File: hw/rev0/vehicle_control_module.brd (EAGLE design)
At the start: 160 x 100 mm, 190 parts, among them IC1 SJA1105TELY, IC10 TJA1100HNZ, IC11 KSZ8061MNXI-TR, IC12 TJA1100HNZ, IC2 ATSAMV71Q21B-AABT, IC3 TJA1100HNZ, IC4 FT2232HL, IC5 TRS3232EQPWRQ1, IC6 AT24MAC402-XHM-B, IC7 DS3231SN#, IC8 TLE9252VSKXUMA1, J1 2305018-2, J10 5-2337992-3, J12 1017505, J2 2305018-2, J3 1017505, J4 1017505, J5 1017505, J6 1017505, J7 1017505, J8 1017505, J9 1017505, U1 122-2920-GR, Y1 NX3225SA-25MHZ-EXS00A-CS11338, Y2 NX2016SA-25.000M-STD-CZS-1

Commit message: Swap EEPROM with QSPI Flash, still has 48-bit EUI
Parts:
- added C64: 1uF, rcl:C0603
- added R78: 0, rcl:R0603
- added R79, R80, R81: 4.7k, rcl:R0603
- IC6: value AT24MAC402-XHM-B -> SST26VF032BT-104I_SM; device samacsys:SOP65P640X120-8N -> samacsys:SOIC127P794X203-8N
- moved IC6 804.9 mm to (-138.4, -853.4)
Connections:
- removed net VCC: IC7.2
- new net EXTINT_RTC: IC2.102, IC7.3, R81.1
- new net FLASH_WP: IC2.41, IC6.3, R78.1
- new net QSPI_QCS: IC2.64, IC6.1
- new net QSPI_QIO0: IC2.42, IC6.5
- new net QSPI_QIO1: IC2.68, IC6.2
- new net QSPI_QSCK: IC2.51, IC6.6
- net +3V3: now also C64.1, IC6.7, IC6.8, IC7.2, R78.2, R79.2, R80.2, R81.2
- net GND: now also C64.2, IC6.4, IC7.10, IC7.11, IC7.12, IC7.5, IC7.6, IC7.7, IC7.8, IC7.9, U1.3
- net I2C0_TWCK: now also IC7.16, R79.1
- net I2C0_TWD: now also IC7.15, R80.1

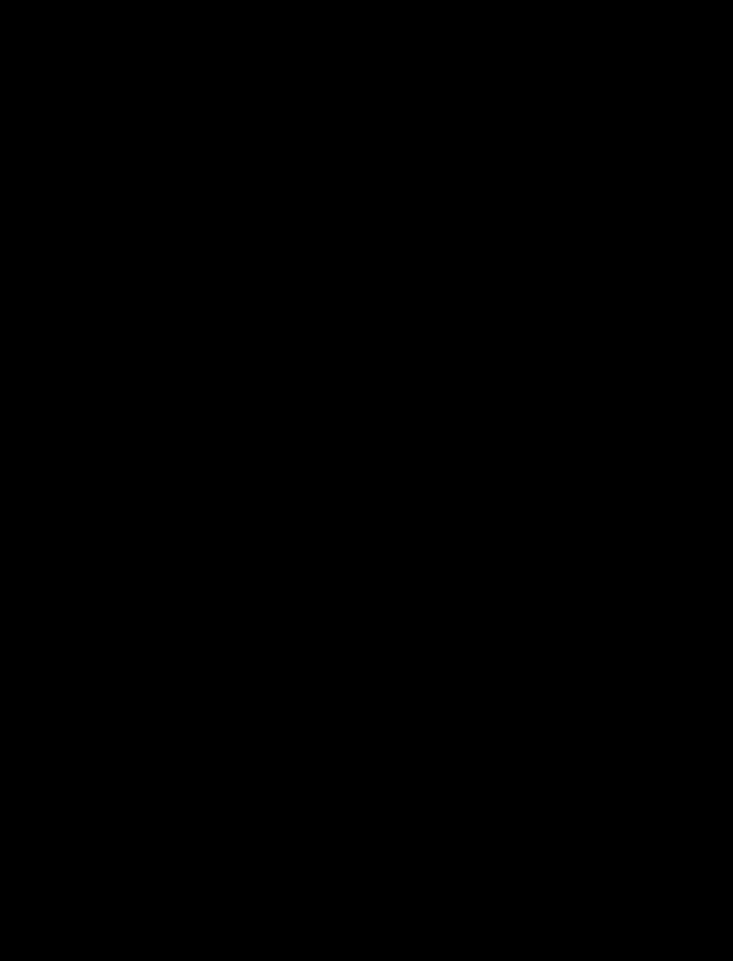
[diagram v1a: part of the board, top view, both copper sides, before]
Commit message: Add JTAG connector
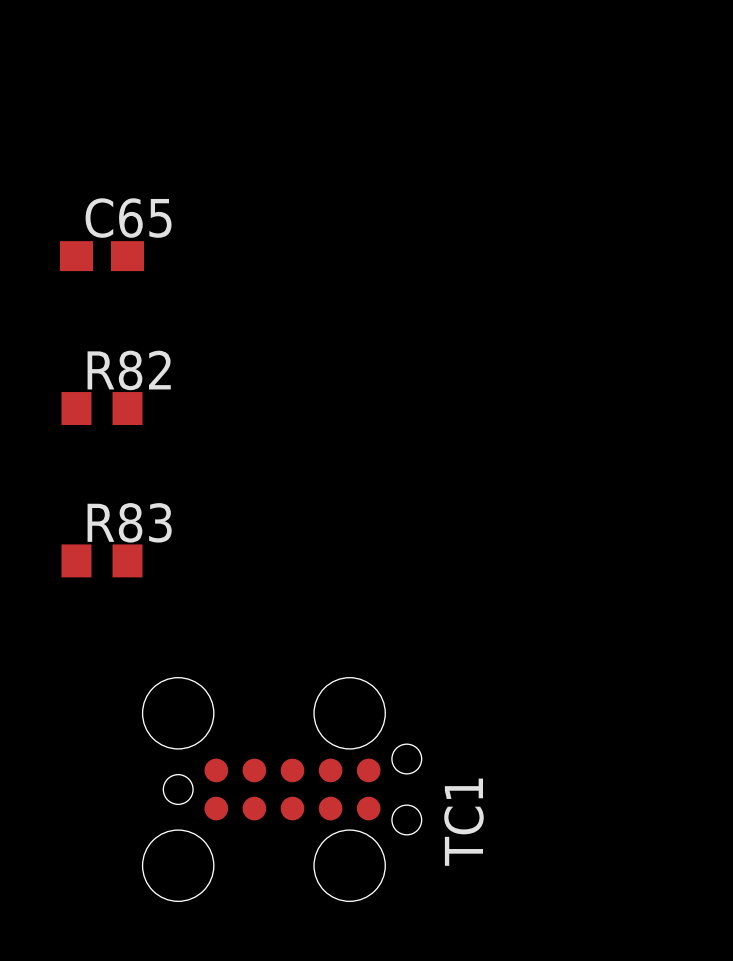
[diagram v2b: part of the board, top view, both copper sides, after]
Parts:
- added C65: 1uF, rcl:C0603
- added R82: 0, rcl:R0603
- added R83: 10k, rcl:R0603
- added TC1: TC2050-IDC, TagConnect:TC2050-IDC
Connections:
- new net HOST_RESET: IC2.83, R82.2, R83.2
- new net JTAG_NRST: R82.1, TC1.10
- new net JTAG_TCK: IC2.89, TC1.4, TC1.7
- new net JTAG_TDI: IC2.105, TC1.8
- new net JTAG_TDO: IC2.109, TC1.6
- new net JTAG_TMS: IC2.79, TC1.2
- new net V+: TC1.5
- net +3V3: now also R83.1, TC1.1
- net GND: now also TC1.3
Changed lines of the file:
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@@
 <layer number="48" name="Document" color="7" fill="1" visible="yes" active="yes"/>
 <layer number="49" name="Reference" color="7" fill="1" visible="yes" active="yes"/>
+<layer number="50" name="dxf" color="7" fill="1" visible="no" active="no"/>
 <layer number="51" name="tDocu" color="7" fill="1" visible="yes" active="yes"/>
 <layer number="52" name="bDocu" color="7" fill="1" visible="yes" active="yes"/>
@@
 <layer number="97" name="Info" color="7" fill="1" visible="no" active="no"/>
 <layer number="98" name="Guide" color="6" fill="1" visible="no" active="no"/>
+<layer number="200" name="200bmp" color="1" fill="10" visible="no" active="no"/>
+<layer number="250" name="Descript" color="3" fill="1" visible="no" active="no"/>
+<layer number="251" name="SMDround" color="12" fill="11" visible="no" active="no"/>
 </layers>
 <board>
@@
 <attribute name="VALUE" x="-138.43" y="-853.44" size="1.27" layer="27" align="center"/>
 </element>
+<element name="C65" library="rcl" library_urn="urn:adsk.eagle:library:334" package="C0603" package3d_urn="urn:adsk.eagle:package:23616/2" value="1uF" x="-149.86" y="-867.41" smashed="yes">
+<attribute name="NAME" x="-150.495" y="-866.775" size="1.27" layer="25"/>
+<attribute name="POPULARITY" value="37" x="-149.86" y="-867.41" size="1.778" layer="27" display="off"/>
+<attribute name="SPICEPREFIX" value="C" x="-149.86" y="-867.41" size="1.778" layer="27" display="off"/>
+<attribute name="VALUE" x="-150.495" y="-869.315" size="1.27" layer="27"/>
+</element>
+<element name="R82" library="rcl" library_urn="urn:adsk.eagle:library:334" package="R0603" package3d_urn="urn:adsk.eagle:package:23555/3" value="0" x="-149.86" y="-872.49" smashed="yes">
+<attribute name="NAME" x="-150.495" y="-871.855" size="1.27" layer="25"/>
+<attribute name="POPULARITY" value="77" x="-149.86" y="-872.49" size="1.778" layer="27" display="off"/>
+<attribute name="SPICEPREFIX" value="R" x="-149.86" y="-872.49" size="1.778" layer="27" display="off"/>
+<attribute name="VALUE" x="-150.495" y="-874.395" size="1.27" layer="27"/>
+</element>
+<element name="R83" library="rcl" library_urn="urn:adsk.eagle:library:334" package="R0603" package3d_urn="urn:adsk.eagle:package:23555/3" value="10k" x="-149.86" y="-877.57" smashed="yes">
+<attribute name="NAME" x="-150.495" y="-876.935" size="1.27" layer="25"/>
+<attribute name="POPULARITY" value="77" x="-149.86" y="-877.57" size="1.778" layer="27" display="off"/>
+<attribute name="SPICEPREFIX" value="R" x="-149.86" y="-877.57" size="1.778" layer="27" display="off"/>
+<attribute name="VALUE" x="-150.495" y="-879.475" size="1.27" layer="27"/>
+</element>
+<element name="TC1" library="TagConnect" package="TC2050-IDC" value="TC2050-IDC" x="-143.51" y="-885.19" smashed="yes">
+<attribute name="NAME" x="-137.16" y="-887.73" size="1.27" layer="25" rot="R90"/>
+<attribute name="VALUE" x="-149.225" y="-887.73" size="1.27" layer="27" rot="R90"/>
+</element>
 </elements>
 <signals>
@@
 <contactref element="IC6" pad="4"/>
 <contactref element="C64" pad="2"/>
+<contactref element="TC1" pad="3"/>
 <wire x1="-78.22" y1="-415.02" x2="-81.7" y2="-419.1" width="0" layer="19" extent="1-1"/>
 <wire x1="-75.35" y1="-406.4" x2="-78.22" y2="-415.02" width="0" layer="19" extent="1-1"/>
@@
 <wire x1="-140.12" y1="-826.77" x2="-140.12" y2="-811.53" width="0" layer="19" extent="1-1"/>
 <wire x1="-142.08" y1="-855.345" x2="-140.12" y2="-826.77" width="0" layer="19" extent="1-1"/>
+<wire x1="-143.51" y1="-885.825" x2="-142.08" y2="-855.345" width="0" layer="19" extent="1-1"/>
 <wire x1="-54.242" y1="-301.625" x2="-75.35" y2="-378.46" width="0" layer="19" extent="1-1"/>
 <wire x1="-54.242" y1="-300.355" x2="-54.242" y2="-301.625" width="0" layer="19" extent="1-1"/>
@@
 <contactref element="R78" pad="2"/>
 <contactref element="IC6" pad="7"/>
+<contactref element="R83" pad="1"/>
+<contactref element="TC1" pad="1"/>
 <wire x1="-84.57" y1="-425.45" x2="-80.76" y2="-422.91" width="0" layer="19" extent="1-1"/>
 <wire x1="-78.42" y1="-413.02" x2="-80.76" y2="-422.91" width="0" layer="19" extent="1-1"/>
@@
 <wire x1="-134.78" y1="-851.535" x2="-140.12" y2="-847.09" width="0" layer="19" extent="1-1"/>
 <wire x1="-134.78" y1="-852.805" x2="-134.78" y2="-851.535" width="0" layer="19" extent="1-1"/>
+<wire x1="-150.71" y1="-877.57" x2="-134.78" y2="-852.805" width="0" layer="19" extent="1-1"/>
+<wire x1="-146.05" y1="-885.825" x2="-150.71" y2="-877.57" width="0" layer="19" extent="1-1"/>
 <wire x1="37.79" y1="33.56" x2="-54.242" y2="-294.005" width="0" layer="19" extent="1-1"/>
 </signal>
@@
 <wire x1="5.95" y1="-23.438" x2="-141.82" y2="-831.85" width="0" layer="19" extent="1-1"/>
 </signal>
+<signal name="JTAG_TMS">
+<contactref element="IC2" pad="79"/>
+<contactref element="TC1" pad="2"/>
+<wire x1="23.438" y1="-18.45" x2="-144.78" y2="-885.825" width="0" layer="19" extent="1-1"/>
+</signal>
+<signal name="JTAG_TCK">
+<contactref element="IC2" pad="89"/>
+<contactref element="TC1" pad="4"/>
+<contactref element="TC1" pad="7"/>
+<wire x1="-142.24" y1="-885.825" x2="23.438" y2="-13.45" width="0" layer="19" extent="1-1"/>
+<wire x1="-142.24" y1="-884.555" x2="-142.24" y2="-885.825" width="0" layer="19" extent="1-1"/>
+</signal>
+<signal name="JTAG_TDO">
+<contactref element="IC2" pad="109"/>
+<contactref element="TC1" pad="6"/>
+<wire x1="-140.97" y1="-884.555" x2="21.45" y2="-1.962" width="0" layer="19" extent="1-1"/>
+</signal>
+<signal name="JTAG_TDI">
+<contactref element="IC2" pad="105"/>
+<contactref element="TC1" pad="8"/>
+<wire x1="-143.51" y1="-884.555" x2="23.438" y2="-5.45" width="0" layer="19" extent="1-1"/>
+</signal>
+<signal name="JTAG_NRST">
+<contactref element="R82" pad="1"/>
+<contactref element="TC1" pad="10"/>
+<wire x1="-150.71" y1="-872.49" x2="-146.05" y2="-884.555" width="0" layer="19" extent="1-1"/>
+</signal>
+<signal name="HOST_RESET">
+<contactref element="IC2" pad="83"/>
+<contactref element="R82" pad="2"/>
+<contactref element="R83" pad="2"/>
+<wire x1="-149.01" y1="-877.57" x2="23.438" y2="-16.45" width="0" layer="19" extent="1-1"/>
+<wire x1="-149.01" y1="-872.49" x2="-149.01" y2="-877.57" width="0" layer="19" extent="1-1"/>
+</signal>
+<signal name="V+">
+<contactref element="TC1" pad="5"/>
+</signal>
 </signals>

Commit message: Flesh out FTDI and RS232
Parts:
- added C66, C68, C69, C70, C75, C76, C77, C78: 100nF, rcl:C0603
- added C67: 3.3uF, rcl:C0603
- added C71, C72: 4.7uF, rcl:C0603
- added C73, C74: 18nF, rcl:C0603
- added C79, C80, C81, C82: 0.1uF, rcl:C0603
- added J11, J13: 2301843-1, samacsys:23018431
- added LED4, LED5, LED6, LED7: (no value), led:CHIPLED_0603
- added R84: 10k, rcl:R0603
- added R85, R88, R89, R90, R91, R92: 12k, rcl:R0603
- added R86, R87: 5.11k, rcl:R0603
- added Y3: ABM8AIG-12.000MHZ-1Z-T, samacsys:ABM8AIG25000MHZ122ZT3
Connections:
- removed net SHIELD: J1.S1, J1.S2, J1.S3, J1.S4, J2.S1, J2.S2, J2.S3, J2.S4
- new net DEBUG_USB_DM: IC4.7, J2.A7, J2.B7
- new net DEBUG_USB_DP: IC4.8, J2.A6, J2.B6
- new net FTDI_OSCI: C74.1, IC4.2, Y3.3
- new net FTDI_OSCO: C73.1, IC4.3, Y3.1
- new net N$67: J2.A5, R86.2
- new net N$68: J2.B5, R87.2
- new net N$69: IC4.6, R85.1
- new net N$70: IC4.14, R88.2
- new net N$71: LED5.A, R90.2
- new net N$72: LED4.A, R89.2
- new net N$73: LED6.A, R91.2
- new net N$74: LED7.A, R92.2
- new net N$75: C79.1, IC5.1
- new net N$76: C79.2, IC5.3
- new net N$77: C80.1, IC5.4
- new net N$78: C80.2, IC5.5
- new net N$79: C81.1, IC5.6
- new net RS232_PORT0_RX: IC5.13, J11.2
- new net RS232_PORT0_TX: IC5.14, J11.3
- new net RS232_PORT1_RX: IC5.8, J13.2
- new net RS232_PORT1_TX: IC5.7, J13.3
- new net UART0_RX_LED: IC4.29, R89.1
- new net UART0_TX_LED: IC4.30, R90.1
- new net UART1_RX_LED: IC4.54, R91.1
- new net UART1_TX_LED: IC4.55, R92.1
- new net VEE: C67.1, C68.1, C69.1, C70.1, IC4.12, IC4.37, IC4.49, IC4.64
- net +3V3: now also C66.1, C71.1, C72.1, C75.1, C76.1, C77.1, C78.1, C82.1, IC4.20, IC4.31, IC4.4, IC4.42, IC4.50, IC4.56, IC4.9, IC5.16, R88.1
- net GND: now also C66.2, C67.2, C68.2, C69.2, C70.2, C71.2, C72.2, C73.2, C74.2, C75.2, C76.2, C77.2, C78.2, C81.2, C82.2, IC4.1, IC4.10, IC4.11, IC4.13, IC4.15, IC4.25, IC4.35, IC4.47, IC4.5, IC4.51, IC5.15, J1.A1, J1.A12, J1.B1, J1.B12, J1.S1, J1.S2, J1.S3, J1.S4, J11.5, J11.MH1, J11.MH2, J13.5, J13.MH1, J13.MH2, J2.A1, J2.A12, J2.B1, J2.B12, J2.S1, J2.S2, J2.S3, J2.S4, LED4.C, LED5.C, LED6.C, LED7.C, R1.1, R2.1, R85.2, R86.1, R87.1, Y3.2, Y3.4
- net UART0_RXD: now also IC4.16
- net UART0_TXD: now also IC4.17
- net UART1_RXD: now also IC4.38
- net UART1_TXD: now also IC4.39
- net UART2_RXD: now also IC5.12
- net UART2_TXD: now also IC5.11
- net UART3_RXD: now also IC5.9
- net UART3_TXD: now also IC5.10

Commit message: Start adding power supply
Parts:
- added C83, C88: 0.47uF, rcl:C0805
- added C84, C85: 470pF, rcl:C0603
- added C86: UCZ1K151MNQ1MS, samacsys:CAPAE1360X1450N
- added C87: 10uF, rcl:C0805
- added D4, D5: PMEG3030EP,115, samacsys:SODFL4725X110N
- added D7: SMAJ24CA-Q, samacsys:DIONM5127X229N
- added IC13: TPS79133MDBVTEP, samacsys:SOT95P280X145-5N
- added IC9: TPS62242DRVR, samacsys:SON65P200X200X80-7N
- added L7: XAL4020-102MEC, samacsys:XAL40XX
- added R93: 10k, rcl:R0603
- added U2: LM63625, LM63625:PWP0016K_L
- added U3: TPS62007-Q1_DGS_10, TPS62007:DGS10
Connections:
- removed net V+: TC1.5
- new net AGND: U2.10
- new net CBOOT: U2.3
- new net EXT_PWR: D5.2, TC1.5
- new net HOST_USB_VBUS: J1.A4, J1.A9, J1.B4, J1.B9
- new net N$80: C83.1, D4.1, D5.1, L7.1
- new net N$81: C84.2, C85.1
- new net N$82: C86.1, C87.1, C88.1, L7.2, U2.12, U2.13
- new net PAD: U2.17
- new net PGND: U2.16, U3.10
- new net PGND_2: U2.15
- new net SW: U2.2
- new net SW_2: U2.1
- new net VBATT: C84.1, D4.2, D7.2
- new net VCC: U2.4
- net GND: now also C83.2, C85.2, C86.2, C87.2, C88.2, D7.1, U3.3

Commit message: Add LTE modem and flesh out CAN interface
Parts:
- removed J1: 2305018-2, 2305018-2:TE_2305018-2
- added C89: 0.1uF, rcl:C0603
- added C90, C93: 4.7nF, rcl:C0603
- added C91, C92, C94, C95, C98: 100nF, rcl:C0603
- added C96: 1uF, rcl:C0603
- added C97: UCZ1K151MNQ1MS, samacsys:CAPAE1360X1450N
- added IC14, IC16: NUP2202W1T2G, samacsys:SOT65P210X110-6N
- added IC15: TLE9252VSKXUMA1, samacsys:SOIC127P599X173-14N
- added J15: 693022010811, samacsys:693022010811
- added J27: 2041119-2, samacsys:20411192
- added LED9: (no value), led:CHIPLED_0603
- added R102: 10k, rcl:R0603
- added R94: 1.21k, rcl:R0603
- added R95, R96: 60, rcl:R0805
- R1, R2: value 5.11k -> 60; device rcl:R0603 -> rcl:R0805
- moved R2 830.6 mm to (-219.7, -1143.0)
- moved R1 667.2 mm to (-219.7, 321.3)
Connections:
- removed net HOST_USB_VBUS: J1.A4, J1.A9, J1.B4, J1.B9
- removed net N$2: J1.A5, R1.2
- removed net N$43: IC11.15
- new net CAN0_EN: IC2.37, IC8.6
- new net CAN0_ERR: IC2.39, IC8.8
- new net CAN0_H: IC14.1, IC8.13, R1.1
- new net CAN0_INH: IC8.7
- new net CAN0_L: IC14.6, IC8.12, R2.2
- new net CAN0_STBY: IC2.38, IC8.14
- new net CAN1_EN: IC15.6, IC2.94
- new net CAN1_ERR: IC15.8, IC2.90
- new net CAN1_H: IC15.13, IC16.1, R95.1
- new net CAN1_INH: IC15.7
- new net CAN1_L: IC15.12, IC16.6, R96.2
- new net CAN1_STBY: IC15.14, IC2.93
- new net MODEM_DISABLE: IC2.142, J27.20
- new net MODEM_RESET: IC2.141, J27.22
- new net MODEM_WAN_LED: J27.42, LED9.C
- new net N$92: LED9.A, R102.2
- new net RTC_RESET: IC2.88, IC7.4
- new net SIM_CLK: J15.3, J27.12
- new net SIM_DATA: J15.7, J27.10
- new net SIM_PWR: J15.1, J15.6, J27.8
- new net SIM_RESET: J15.2, J27.14
- new net VBATT_PROT: C86.1, C87.1, C88.1, IC15.10, IC15.9, IC8.10, IC8.9, L7.2, R93.1, U2.12, U2.13
- net +3V3: now also C91.1, C92.1, C94.1, C95.1, C96.1, C97.1, C98.1, IC11.15, IC14.5, IC15.3, IC15.5, IC16.5, IC8.3, IC8.5, J27.2, J27.24, J27.39, J27.41, J27.52, R102.1
- net ADC0_0: now also C89.1, R93.2, R94.2
- net CAN0_RX: now also IC8.4
- net CAN0_TX: now also IC8.1
- net CAN1_RX: now also IC15.4
- net CAN1_TX: now also IC15.1
- net GND: now also C89.2, C90.2, C91.2, C92.2, C93.2, C94.2, C95.2, C96.2, C97.2, C98.2, IC14.2, IC15.2, IC16.2, IC2.115, IC2.135, IC2.138, IC2.44, IC2.61, IC2.95, IC8.2, J15.5, J27.15, J27.18, J27.21, J27.26, J27.27, J27.29, J27.34, J27.35, J27.37, J27.4, J27.40, J27.43, J27.45, J27.50, J27.9, R94.1; no longer J1.A1, J1.A12, J1.B1, J1.B12, J1.G1, J1.G2, J1.S1, J1.S2, J1.S3, J1.S4, R1.1, R2.1
- net HOST_USB_DM: now also J27.36; no longer J1.A7, J1.B7
- net HOST_USB_DP: now also J27.38; no longer J1.A6, J1.B6
- net N$3: now also C93.1, R95.2, R96.1; no longer J1.B5, R2.2
- net N$82: now also C90.1, R1.2, R2.1; no longer C86.1, C87.1, C88.1, L7.2, U2.12, U2.13

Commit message: First stab at power supply
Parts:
- added C100, C99: 470pF, rcl:C0805
- added C101: 0.47uF, rcl:C0603
- added C102: 220nF, rcl:C0805
- added C103, C104, C105, C107: 10uF, rcl:C0805
- added C106, C109: 1uF, rcl:C0603
- added C108: 0.01uF, rcl:C0603
- added C110: 0.1uF, rcl:C0603
- added D6, D9: PMEG3030EP,115, samacsys:SODFL4725X110N
- added D8: SMAJ24CA-Q, samacsys:DIONM5127X229N
- added L10: LPS3015-222MRB, samacsys:LPS3015
- added L8: XAL4040-103MEC, samacsys:XAL40XX
- added L9: DO3316P-103MLB, samacsys:DO3316P103MLB
- added R100, R101: 1k, rcl:R0603
- added R97: 1k, rcl:R0805
- added R98: 10k, rcl:R0603
- added R99: 0, rcl:R0603
- C84, C85: device rcl:C0603 -> rcl:C0805
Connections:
- removed net AGND: U2.10
- removed net CAN0_INH: IC8.7
- removed net CAN1_INH: IC15.7
- removed net CBOOT: U2.3
- removed net PAD: U2.17
- removed net PGND: U2.16, U3.10
- removed net PGND_2: U2.15
- removed net SW: U2.2
- removed net SW_2: U2.1
- removed net VCC: U2.4
- new net +5V: C103.1, C107.1, C110.1, IC13.1, IC9.5, L8.2, U2.9, U3.1, U3.6
- new net 1V2_SUPPLY_EN: IC9.4, R100.2
- new net 3V3_AD_REF: C109.1, IC13.5
- new net 3V3_AD_SUPPLY_EN: IC13.3, R101.2
- new net MAIN_SUPPLY_PGOOD: R98.1, U2.8, U3.8
- new net N$2: C100.1, C99.2
- new net N$43: D6.1, D9.1, R97.2, U2.11
- new net N$83: C101.1, R98.2, U2.4, U2.5, U2.6
- new net N$84: L9.2, U3.9
- new net N$85: C102.2, L8.1, U2.1, U2.2
- new net N$86: C106.1, U3.2
- new net N$87: C102.1, U2.3
- new net N$88: R99.1, U3.4
- new net N$89: IC9.1, L10.2
- new net N$90: C108.1, IC13.4
- new net SWITCHED_IGN: C99.1, D6.2, D8.2
- net +3V3: now also C105.1, L9.1, U3.5
- net EXT_PWR: now also D9.2
- net GND: now also C100.2, C101.2, C103.2, C104.2, C105.2, C106.2, C107.2, C108.2, C109.2, C110.2, D8.1, IC13.2, IC9.2, IC9.6, IC9.7, R100.1, R101.1, R97.1, U2.10, U2.15, U2.16, U2.17, U2.7, U3.10, U3.7
- net HOST_RESET: now also R99.2
- net VDD: now also C104.1, IC9.3, L10.1

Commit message: Switch 3V3 LDO to fix compatibility with EN pins
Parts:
- removed C108: 0.01uF, rcl:C0603
- removed IC13: TPS79133MDBVTEP, samacsys:SOT95P280X145-5N
- removed R100, R101: 1k, rcl:R0603
- added IC17: LP5907QMFX-3.3Q1, samacsys:SOT95P280X145-5N
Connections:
- net N$88 renamed 3V3_SUPPLY_PGOOD
- removed net 1V2_SUPPLY_EN: IC9.4, R100.2
- removed net 3V3_AD_SUPPLY_EN: IC13.3, R101.2
- removed net MAIN_SUPPLY_PGOOD: R98.1, U2.8, U3.8
- removed net N$90: C108.1, IC13.4
- new net 5V_SUPPLY_PGOOD: IC17.3, IC9.4, R98.1, U2.8, U3.8
- net +5V: now also IC17.1; no longer IC13.1
- net 3V3_AD_REF: now also IC17.5; no longer IC13.5
- net GND: now also IC17.2; no longer C108.2, IC13.2, R100.1, R101.1
